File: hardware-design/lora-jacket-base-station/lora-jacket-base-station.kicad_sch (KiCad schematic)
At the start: 6 parts, among them J1 RC522 CONNECTOR, U1 NODEMCU-32S, U2 RA-01H

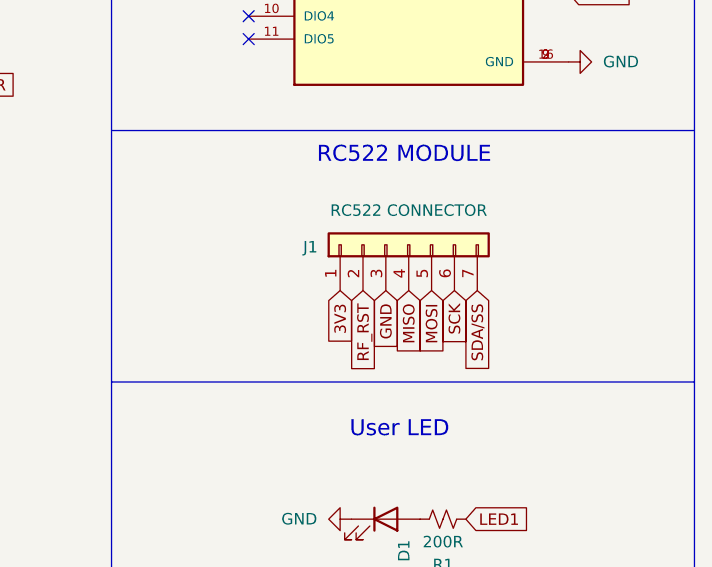
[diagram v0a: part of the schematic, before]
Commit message: adds base station PCB
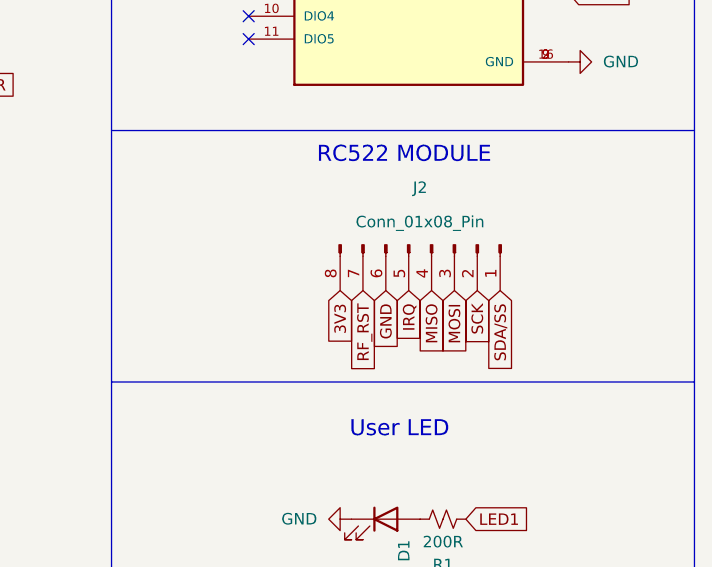
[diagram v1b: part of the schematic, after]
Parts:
- removed J1: RC522 CONNECTOR, symbol Connector_Generic:Conn_01x07
- added J2: Conn_01x08_Pin, Connector_PinHeader_2.54mm:PinHeader_1x08_P2.54mm_Vertical, symbol Connector:Conn_01x08_Pin
- BZ1: footprint (none) -> Buzzer_Beeper:MagneticBuzzer_ProSignal_ABI-010-RC
- D1: footprint (none) -> LED_THT:LED_D3.0mm
- R1: footprint (none) -> Resistor_THT:R_Axial_DIN0516_L15.5mm_D5.0mm_P25.40mm_Horizontal
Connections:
- net 3V3: now also J2.8 (Pin_8)
- net GND: now also J2.6 (Pin_6)
- net MISO: now also J2.4 (Pin_4)
- net MOSI: now also J2.3 (Pin_3)
- net RF_RST: now also J2.7 (Pin_7)
- net SCK: now also J2.2 (Pin_2)
- net SDA/SS: now also J2.1 (Pin_1)
- new net IRQ: J2.5 (Pin_5)
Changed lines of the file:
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@@
+		)
+	)
+	(global_label "IRQ"
+		(shape input)
+		(at 195.58 130.81 270)
+		(fields_autoplaced yes)
+		(effects
+			(font
+				(size 1.27 1.27)
+			)
+			(justify right)
+		)
+		(property "Intersheetrefs" "${INTERSHEET_REFS}"
+			(at 195.58 136.2788 90)
+			(effects
+				(font
+					(size 1.27 1.27)
+				)
+				(justify right)
+				(hide yes)
+			)
 		)
 	)
@@
 	(global_label "MISO"
 		(shape input)
-		(at 195.58 130.81 270)
+		(at 198.12 130.81 270)
 		(fields_autoplaced yes)
 		(effects
@@
 		)
 		(property "Intersheetrefs" "${INTERSHEET_REFS}"
-			(at 195.58 137.6908 90)
+			(at 198.12 137.6908 90)
 			(effects
 				(font
@@
 	(global_label "SDA{slash}SS"
 		(shape input)
+		(at 205.74 130.81 270)
+		(fields_autoplaced yes)
+		(effects
+			(font
+				(size 1.27 1.27)
+			)
+			(justify right)
+		)
+		(property "Intersheetrefs" "${INTERSHEET_REFS}"
+			(at 205.74 139.542 90)
+			(effects
+				(font
+					(size 1.27 1.27)
+				)
+				(justify right)
+				(hide yes)
+			)
+		)
+	)
+	(global_label "LORA_RST"
+		(shape input)
+		(at 142.24 72.39 0)
+		(fields_autoplaced yes)
+		(effects
+			(font
+				(size 1.27 1.27)
+			)
+			(justify left)
+		)
+		(property "Intersheetrefs" "${INTERSHEET_REFS}"
+			(at 153.1632 72.39 0)
+			(effects
+				(font
+					(size 1.27 1.27)
+				)
+				(justify left)
+				(hide yes)
+			)
+		)
+	)
+	(global_label "LED1"
+		(shape input)
+		(at 142.24 110.49 0)
+		(fields_autoplaced yes)
+		(effects
+			(font
+				(size 1.27 1.27)
+			)
+			(justify left)
+		)
+		(property "Intersheetrefs" "${INTERSHEET_REFS}"
+			(at 149.0067 110.49 0)
+			(effects
+				(font
+					(size 1.27 1.27)
+				)
+				(justify left)
+				(hide yes)
+			)
+		)
+	)
+	(global_label "SDA{slash}SS"
+		(shape input)
+		(at 142.24 77.47 0)
+		(fields_autoplaced yes)
+		(effects
+			(font
+				(size 1.27 1.27)
+			)
+			(justify left)
+		)
+		(property "Intersheetrefs" "${INTERSHEET_REFS}"
+			(at 150.972 77.47 0)
+			(effects
+				(font
+					(size 1.27 1.27)
+				)
+				(justify left)
+				(hide yes)
+			)
+		)
+	)
+	(global_label "MOSI"
+		(shape input)
+		(at 200.66 130.81 270)
+		(fields_autoplaced yes)
+		(effects
+			(font
+				(size 1.27 1.27)
+			)
+			(justify right)
+		)
+		(property "Intersheetrefs" "${INTERSHEET_REFS}"
+			(at 200.66 137.7082 90)
+			(effects
+				(font
+					(size 1.27 1.27)
+				)
+				(justify right)
+				(hide yes)
+			)
+		)
+	)
+	(global_label "SCK"
+		(shape input)
 		(at 203.2 130.81 270)
 		(fields_autoplaced yes)
@@
 		)
 		(property "Intersheetrefs" "${INTERSHEET_REFS}"
-			(at 203.2 139.542 90)
-			(effects
-				(font
-					(size 1.27 1.27)
-				)
-				(justify right)
-				(hide yes)
-			)
-		)
-	)
-	(global_label "LORA_RST"
-		(shape input)
-		(at 142.24 72.39 0)
-		(fields_autoplaced yes)
-		(effects
-			(font
-				(size 1.27 1.27)
-			)
-			(justify left)
-		)
-		(property "Intersheetrefs" "${INTERSHEET_REFS}"
-			(at 153.1632 72.39 0)
-			(effects
-				(font
-					(size 1.27 1.27)
-				)
-				(justify left)
-				(hide yes)
-			)
-		)
-	)
-	(global_label "LED1"
-		(shape input)
-		(at 142.24 110.49 0)
-		(fields_autoplaced yes)
-		(effects
-			(font
-				(size 1.27 1.27)
-			)
-			(justify left)
-		)
-		(property "Intersheetrefs" "${INTERSHEET_REFS}"
-			(at 149.0067 110.49 0)
-			(effects
-				(font
-					(size 1.27 1.27)
-				)
-				(justify left)
-				(hide yes)
-			)
-		)
-	)
-	(global_label "SDA{slash}SS"
-		(shape input)
-		(at 142.24 77.47 0)
-		(fields_autoplaced yes)
-		(effects
-			(font
-				(size 1.27 1.27)
-			)
-			(justify left)
-		)
-		(property "Intersheetrefs" "${INTERSHEET_REFS}"
-			(at 150.972 77.47 0)
-			(effects
-				(font
-					(size 1.27 1.27)
-				)
-				(justify left)
-				(hide yes)
-			)
-		)
-	)
-	(global_label "MOSI"
-		(shape input)
-		(at 198.12 130.81 270)
-		(fields_autoplaced yes)
-		(effects
-			(font
-				(size 1.27 1.27)
-			)
-			(justify right)
-		)
-		(property "Intersheetrefs" "${INTERSHEET_REFS}"
-			(at 198.12 137.7082 90)
-			(effects
-				(font
-					(size 1.27 1.27)
-				)
-				(justify right)
-				(hide yes)
-			)
-		)
-	)
-	(global_label "SCK"
-		(shape input)
-		(at 200.66 130.81 270)
-		(fields_autoplaced yes)
-		(effects
-			(font
-				(size 1.27 1.27)
-			)
-			(justify right)
-		)
-		(property "Intersheetrefs" "${INTERSHEET_REFS}"
-			(at 200.66 136.6002 90)
+			(at 203.2 136.6002 90)
 			(effects
 				(font
@@
 			)
 		)
-		(property "Footprint" ""
+		(property "Footprint" "Buzzer_Beeper:MagneticBuzzer_ProSignal_ABI-010-RC"
 			(at 188.595 59.69 90)
 			(effects
@@
 			)
 		)
-		(property "Footprint" ""
+		(property "Footprint" "LED_THT:LED_D3.0mm"
 			(at 193.04 156.21 0)
 			(effects
@@
 	)
 	(symbol
-		(lib_id "Connector_Generic:Conn_01x07")
-		(at 195.58 125.73 90)
-		(unit 1)
-		(exclude_from_sim no)
-		(in_bom yes)
-		(on_board yes)
-		(dnp no)
-		(property "Reference" "J1"
-			(at 184.658 125.984 90)
-			(effects
-				(font
-					(size 1.27 1.27)
-				)
-			)
-		)
-		(property "Value" "RC522 CONNECTOR"
-			(at 195.58 121.92 90)
-			(effects
-				(font
-					(size 1.27 1.27)
-				)
-			)
-		)
-		(property "Footprint" ""
-			(at 195.58 125.73 0)
-			(effects
-				(font
-					(size 1.27 1.27)
-				)
-				(hide yes)
-			)
-		)
-		(property "Datasheet" "~"
-			(at 195.58 125.73 0)
-			(effects
-				(font
-					(size 1.27 1.27)
-				)
-				(hide yes)
-			)
-		)
-		(property "Description" "Generic connector, single row, 01x07, script generated (kicad-library-utils/schlib/autogen/connector/)"
-			(at 195.58 125.73 0)
-			(effects
-				(font
-					(size 1.27 1.27)
-				)
-				(hide yes)
-			)
-		)
-		(pin "6"
-		)
-		(pin "3"
-		)
-		(pin "5"
-		)
-		(pin "1"
-		)
-		(pin "7"
-		)
-		(pin "2"
-		)
-		(pin "4"
-		)
-		(instances
-			(project "lora-jacket-base-station"
-				(path "/4b3c1ad1-725c-4035-8503-3911e6a04a0d"
-					(reference "J1")
-					(unit 1)
-				)
-			)
-		)
-	)
-	(symbol
 		(lib_id "power:GND")
 		(at 189.23 156.21 270)
@@
 				(path "/4b3c1ad1-725c-4035-8503-3911e6a04a0d"
 					(reference "#PWR04")
+					(unit 1)
+				)
+			)
+		)
+	)
+	(symbol
+		(lib_id "Connector:Conn_01x08_Pin")
+		(at 198.12 125.73 270)
+		(unit 1)
+		(exclude_from_sim no)
+		(in_bom yes)
+		(on_board yes)
+		(dnp no)
+		(property "Reference" "J2"
+			(at 196.85 119.38 90)
+			(effects
+				(font
+					(size 1.27 1.27)
+				)
+			)
+		)
+		(property "Value" "Conn_01x08_Pin"
+			(at 196.85 123.19 90)
+			(effects
+				(font
+					(size 1.27 1.27)
+				)
+			)
+		)
+		(property "Footprint" "Connector_PinHeader_2.54mm:PinHeader_1x08_P2.54mm_Vertical"
+			(at 198.12 125.73 0)
+			(effects
+				(font
+					(size 1.27 1.27)
+				)
+				(hide yes)
+			)
+		)
+		(property "Datasheet" "~"
+			(at 198.12 125.73 0)
+			(effects
+				(font
+					(size 1.27 1.27)
+				)
+				(hide yes)
+			)
+		)
+		(property "Description" "Generic connector, single row, 01x08, script generated"
+			(at 198.12 125.73 0)
+			(effects
+				(font
+					(size 1.27 1.27)
+				)
+				(hide yes)
+			)
+		)
+		(pin "1"
+		)
+		(pin "4"
+		)
+		(pin "2"
+		)
+		(pin "6"
+		)
+		(pin "3"
+		)
+		(pin "5"
+		)
+		(pin "7"
+		)
+		(pin "8"
+		)
+		(instances
+			(project ""
+				(path "/4b3c1ad1-725c-4035-8503-3911e6a04a0d"
+					(reference "J2")
 					(unit 1)
 				)
@@
 			)
 		)
-		(property "Footprint" ""
+		(property "Footprint" "Resistor_THT:R_Axial_DIN0516_L15.5mm_D5.0mm_P25.40mm_Horizontal"
 			(at 199.39 156.21 0)
 			(effects
